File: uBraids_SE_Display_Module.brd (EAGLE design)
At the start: 40 x 25 mm, 39 parts, among them Q1 NPN-SOT323-BEC, Q2 NPN-SOT323-BEC, Q3 NPN-SOT323-BEC, Q4 NPN-SOT323-BEC, U1 SN74HC595-TSSOP-16, U2 SN74HC595-TSSOP-16

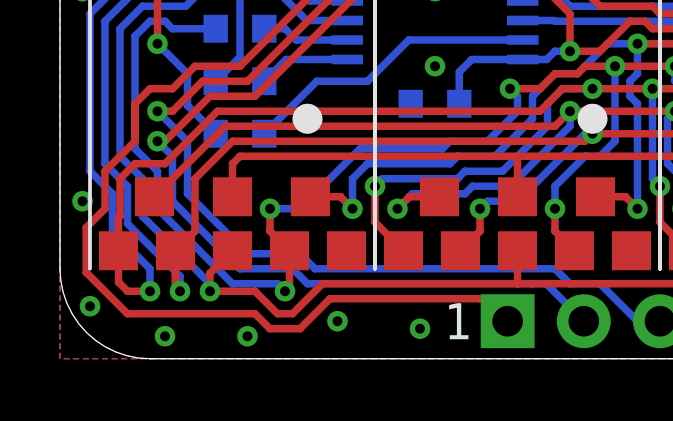
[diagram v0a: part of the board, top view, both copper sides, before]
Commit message: revision C first pass, primarily to address rail clearance
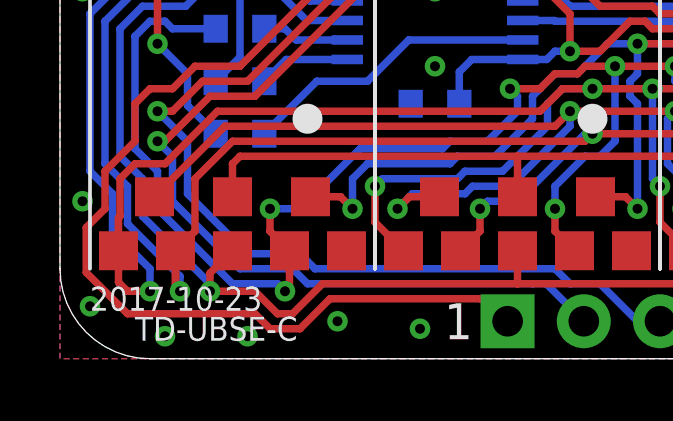
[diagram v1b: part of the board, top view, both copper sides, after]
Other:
- board text added: "2017-10-23"
- board text added: "TALL-DOG.COM 2017-10-23 TD-UBSE-C"
- board text added: "TD-UBSE-C"
- board text removed: "TALL-DOG.COM 4x14-SEGMENT 2017-06-05"
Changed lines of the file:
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@@
 <?xml version="1.0" encoding="utf-8"?>
 <!DOCTYPE eagle SYSTEM "eagle.dtd">
-<eagle version="8.2.1">
+<eagle version="8.4.0">
 <drawing>
 <settings>
 <setting alwaysvectorfont="yes"/>
+<setting keepoldvectorfont="yes"/>
 <setting verticaltext="up"/>
 </settings>
@@
 <layer number="20" name="Dimension" color="15" fill="1" visible="yes" active="yes"/>
 <layer number="21" name="tPlace" color="7" fill="1" visible="yes" active="yes"/>
-<layer number="22" name="bPlace" color="7" fill="1" visible="yes" active="yes"/>
+<layer number="22" name="bPlace" color="14" fill="1" visible="yes" active="yes"/>
 <layer number="23" name="tOrigins" color="15" fill="1" visible="yes" active="yes"/>
 <layer number="24" name="bOrigins" color="15" fill="1" visible="yes" active="yes"/>
@@
 <text x="26.5" y="1.25" size="1.2" layer="21" ratio="12" align="center-left">5</text>
 <text x="12.25" y="3.25" size="1" layer="22" ratio="10" rot="MR0" align="center-left">TALL-DOG.COM
-4x14-SEGMENT
-2017-06-05</text>
+2017-10-23
+TD-UBSE-C</text>
 <text x="30.25" y="17.125" size="1" layer="22" ratio="10" rot="MR90" align="center">DC4</text>
 <text x="28.25" y="17.125" size="1" layer="22" ratio="10" rot="MR90" align="center">GND</text>
@@
 <text x="27.5" y="1.25" size="1" layer="22" ratio="10" rot="MR180" align="center">H1</text>
 <text x="32.5" y="23.75" size="1" layer="22" ratio="10" rot="MR180" align="center">H2</text>
+<text x="1" y="2" size="0.8" layer="21" ratio="12" align="center-left">2017-10-23</text>
+<text x="2.5" y="1" size="0.8" layer="21" ratio="12" align="center-left">TD-UBSE-C</text>
 </plain>
 <attributes>
@@
 <param name="dpMaxLengthDifference" value="10mm"/>
 <param name="dpGapFactor" value="2.5"/>
-<param name="checkGrid" value="0"/>
-<param name="checkAngle" value="1"/>
 <param name="checkFont" value="1"/>
 <param name="checkRestrict" value="1"/>
+<param name="checkStop" value="0"/>
 <param name="useDiameter" value="13"/>
 <param name="maxErrors" value="50"/>

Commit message: prep for production of revision C
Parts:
- removed U$7: (no value), uBraids_SE:OSH-LOGO-5MM
- added U$8: (no value), uBraids_SE:MARKING-CC-LOGO
- added U$9: (no value), uBraids_SE:MARKING-OSH-LOGO-5MM
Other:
- board text added: "2017-10-24"
- board text added: "TALL-DOG.COM 2017-10-24 TD-UBSE-C"
- board text removed: "2017-10-23"
- board text removed: "BY-SA 4.0"
- board text removed: "CC"
- board text removed: "TALL-DOG.COM 2017-10-23 TD-UBSE-C"
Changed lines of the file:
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@@
 <settings>
 <setting alwaysvectorfont="yes"/>
-<setting keepoldvectorfont="yes"/>
 <setting verticaltext="up"/>
 </settings>
@@
 <wire x1="40" y1="3" x2="37" y2="0" width="0" layer="20" curve="-90"/>
 <wire x1="37" y1="25" x2="40" y2="22" width="0" layer="20" curve="-90"/>
-<text x="8.75" y="23.75" size="1.2" layer="21" ratio="12" align="center-right">14</text>
-<text x="31.5" y="23.75" size="1.2" layer="21" ratio="12" align="center-left">6</text>
-<text x="13.75" y="1.25" size="1.2" layer="21" ratio="12" align="center-right">1</text>
-<text x="26.5" y="1.25" size="1.2" layer="21" ratio="12" align="center-left">5</text>
-<text x="12.25" y="3.25" size="1" layer="22" ratio="10" rot="MR0" align="center-left">TALL-DOG.COM
-2017-10-23
+<text x="8.5" y="23.75" size="1.2" layer="21" ratio="10" align="center-right">14</text>
+<text x="31.5" y="23.75" size="1.2" layer="21" ratio="10" align="center-left">6</text>
+<text x="13.5" y="1.25" size="1.2" layer="21" ratio="10" align="center-right">1</text>
+<text x="26.5" y="1.25" size="1.2" layer="21" ratio="10" align="center-left">5</text>
+<text x="12.5" y="3.5" size="1.1" layer="22" ratio="10" rot="MR0" align="center-left">TALL-DOG.COM
+2017-10-24
 TD-UBSE-C</text>
-<text x="30.25" y="17.125" size="1" layer="22" ratio="10" rot="MR90" align="center">DC4</text>
-<text x="28.25" y="17.125" size="1" layer="22" ratio="10" rot="MR90" align="center">GND</text>
-<text x="26.25" y="17.125" size="1" layer="22" ratio="10" rot="MR90" align="center">GND</text>
-<text x="24.25" y="17.125" size="1" layer="22" ratio="10" rot="MR90" align="center">DC3</text>
-<text x="22.25" y="17.125" size="1" layer="22" ratio="10" rot="MR90" align="center">GND</text>
-<text x="20.25" y="17.125" size="1" layer="22" ratio="10" rot="MR90" align="center">GND</text>
-<text x="18.25" y="17.125" size="1" layer="22" ratio="10" rot="MR90" align="center">GND</text>
-<text x="16.25" y="17.125" size="1" layer="22" ratio="10" rot="MR90" align="center">DC2</text>
-<text x="14.25" y="17.125" size="1" layer="22" ratio="10" rot="MR90" align="center">DC1</text>
+<text x="30.25" y="17" size="1" layer="22" ratio="10" rot="MR90" align="center">DC4</text>
+<text x="28.25" y="17" size="1" layer="22" ratio="10" rot="MR90" align="center">GND</text>
+<text x="26.25" y="17" size="1" layer="22" ratio="10" rot="MR90" align="center">GND</text>
+<text x="24.25" y="17" size="1" layer="22" ratio="10" rot="MR90" align="center">DC3</text>
+<text x="22.25" y="17" size="1" layer="22" ratio="10" rot="MR90" align="center">GND</text>
+<text x="20.25" y="17" size="1" layer="22" ratio="10" rot="MR90" align="center">GND</text>
+<text x="18.25" y="17" size="1" layer="22" ratio="10" rot="MR90" align="center">GND</text>
+<text x="16.25" y="17" size="1" layer="22" ratio="10" rot="MR90" align="center">DC2</text>
+<text x="14.25" y="17" size="1" layer="22" ratio="10" rot="MR90" align="center">DC1</text>
 <text x="25.08" y="2.875" size="1" layer="22" ratio="10" rot="MR90" align="center-left">3V3</text>
 <text x="22.54" y="2.875" size="1" layer="22" ratio="10" rot="MR90" align="center-left">GND</text>
@@
 <wire x1="29.25" y1="18.75" x2="29.25" y2="15.25" width="0.127" layer="22"/>
 <wire x1="30.25" y1="22.45" x2="30.25" y2="18.75" width="0.127" layer="22"/>
-<circle x="19.5" y="11" radius="2.2" width="0.35" layer="22"/>
-<text x="19.34" y="11" size="1.6" layer="22" ratio="15" rot="MR0" align="center">CC</text>
-<text x="19.5" y="7.25" size="0.75" layer="22" ratio="12" rot="MR0" align="center">BY-SA
-4.0</text>
-<text x="27.5" y="1.25" size="1" layer="22" ratio="10" rot="MR180" align="center">H1</text>
-<text x="32.5" y="23.75" size="1" layer="22" ratio="10" rot="MR180" align="center">H2</text>
-<text x="1" y="2" size="0.8" layer="21" ratio="12" align="center-left">2017-10-23</text>
-<text x="2.5" y="1" size="0.8" layer="21" ratio="12" align="center-left">TD-UBSE-C</text>
+<text x="26.75" y="1.25" size="1" layer="22" ratio="10" rot="MR180" align="center-left">H1</text>
+<text x="31.75" y="23.75" size="1" layer="22" ratio="10" rot="MR180" align="center-left">H2</text>
+<text x="2.25" y="1" size="0.9" layer="21" ratio="10" align="center-left">TD-UBSE-C</text>
+<text x="1" y="2.25" size="0.9" layer="21" ratio="10" align="center-left">2017-10-24</text>
 </plain>
 <attributes>
@@
 <attribute name="NAME" x="36.25" y="3.75" size="0.5" layer="52" ratio="10" rot="MR0" align="center"/>
 </element>
-<element name="R13" library="uBraids_SE" package="0603-NP" value="100R" x="6" y="7.5" rot="MR0"/>
-<element name="R14" library="uBraids_SE" package="0603-NP" value="100R" x="6" y="9.25" rot="MR0"/>
-<element name="R15" library="uBraids_SE" package="0603-NP" value="100R" x="6" y="11" rot="MR0"/>
-<element name="R16" library="uBraids_SE" package="0603-NP" value="100R" x="6" y="12.75" rot="MR0"/>
-<element name="R17" library="uBraids_SE" package="0603-NP" value="100R" x="6" y="14.5" rot="MR0"/>
-<element name="R18" library="uBraids_SE" package="0603-NP" value="100R" x="6" y="16.25" rot="MR0"/>
+<element name="R13" library="uBraids_SE" package="0603-NP" value="100R" x="6" y="7.5" smashed="yes" rot="MR0">
+<attribute name="NAME" x="4.25" y="7.5" size="1" layer="22" ratio="10" rot="MR0" align="center-left"/>
+<attribute name="NAME" x="6" y="7.5" size="0.5" layer="52" ratio="10" rot="MR180" align="center"/>
+</element>
+<element name="R14" library="uBraids_SE" package="0603-NP" value="100R" x="6" y="9.25" smashed="yes" rot="MR0">
+<attribute name="NAME" x="4.25" y="9.25" size="1" layer="22" ratio="10" rot="MR0" align="center-left"/>
+<attribute name="NAME" x="6" y="9.25" size="0.5" layer="52" ratio="10" rot="MR180" align="center"/>
+</element>
+<element name="R15" library="uBraids_SE" package="0603-NP" value="100R" x="6" y="11" smashed="yes" rot="MR0">
+<attribute name="NAME" x="4.25" y="11" size="1" layer="22" ratio="10" rot="MR0" align="center-left"/>
+<attribute name="NAME" x="6" y="11" size="0.5" layer="52" ratio="10" rot="MR180" align="center"/>
+</element>
+<element name="R16" library="uBraids_SE" package="0603-NP" value="100R" x="6" y="12.75" smashed="yes" rot="MR0">
+<attribute name="NAME" x="4.25" y="12.75" size="1" layer="22" ratio="10" rot="MR0" align="center-left"/>
+<attribute name="NAME" x="6" y="12.75" size="0.5" layer="52" ratio="10" rot="MR180" align="center"/>
+</element>
+<element name="R17" library="uBraids_SE" package="0603-NP" value="100R" x="6" y="14.5" smashed="yes" rot="MR0">
+<attribute name="NAME" x="4.25" y="14.5" size="1" layer="22" ratio="10" rot="MR0" align="center-left"/>
+<attribute name="NAME" x="6" y="14.5" size="0.5" layer="52" ratio="10" rot="MR180" align="center"/>
+</element>
+<element name="R18" library="uBraids_SE" package="0603-NP" value="100R" x="6" y="16.25" smashed="yes" rot="MR0">
+<attribute name="NAME" x="4.25" y="16.25" size="1" layer="22" ratio="10" rot="MR0" align="center-left"/>
+<attribute name="NAME" x="6" y="16.25" size="0.5" layer="52" ratio="10" rot="MR180" align="center"/>
+</element>
 <element name="H1" library="Headers" package="HEADER-1X05-PTH-2.54-MALE" value="HEADER-1X05-PTH-2.54-MALE" x="20" y="1.25" rot="MR180"/>
 <element name="H2" library="Headers" package="HEADER-1X09-PTH-2.54-MALE" value="HEADER-1X09-PTH-2.54-MALE" x="20" y="23.75" rot="MR0"/>
-<element name="C1" library="uBraids_SE" package="0603-NP" value="0.1uF" x="26.5" y="8" rot="MR180"/>
+<element name="C1" library="uBraids_SE" package="0603-NP" value="0.1uF" x="26.5" y="8" smashed="yes" rot="MR180">
+<attribute name="NAME" x="28.25" y="8" size="1" layer="22" ratio="10" rot="MR180" align="center-left"/>
+<attribute name="NAME" x="26.5" y="8" size="0.5" layer="52" ratio="10" rot="MR0" align="center"/>
+</element>
 <element name="C2" library="uBraids_SE" package="0603-NP" value="0.1uF" x="12.5" y="8.5" smashed="yes" rot="MR0">
 <attribute name="NAME" x="14.25" y="8.5" size="1" layer="22" ratio="10" rot="MR180" align="center-left"/>
@@
 <element name="U$5" library="uBraids_SE" package="FIDUCIAL" value="" x="37.75" y="23.5" rot="MR0"/>
 <element name="U$6" library="uBraids_SE" package="FIDUCIAL" value="" x="34" y="1.25" rot="MR0"/>
-<element name="U$7" library="uBraids_SE" package="OSH-LOGO-5MM" value="" x="10.375" y="17.25" rot="MR0"/>
+<element name="U$8" library="uBraids_SE" package="MARKING-CC-LOGO" value="" x="19.5" y="9.5" rot="MR0"/>
+<element name="U$9" library="uBraids_SE" package="MARKING-OSH-LOGO-5MM" value="" x="10.5" y="17" rot="MR0"/>
 </elements>
 <signals>
